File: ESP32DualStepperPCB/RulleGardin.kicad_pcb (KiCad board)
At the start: 2 copper layers, 56 x 33 mm, 20 parts, among them J1 Power, J2 Prog, J3 Conn_01x05, U1 ESP32-S2-WROVER, U2 TSR_1-2433, U3 ULN2003A, U4 AZ1117-3.3

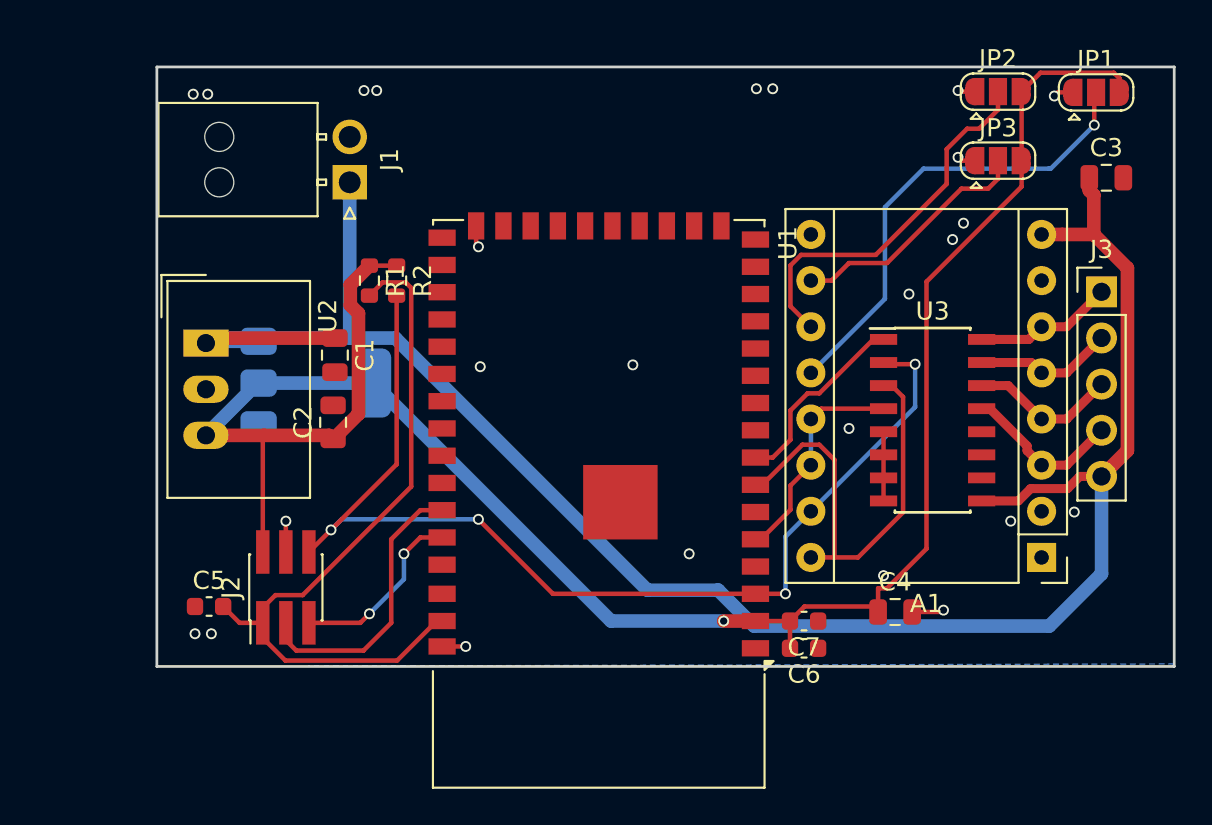
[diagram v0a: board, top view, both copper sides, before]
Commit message: fund that its the dhcp that the problem, so now with static IP
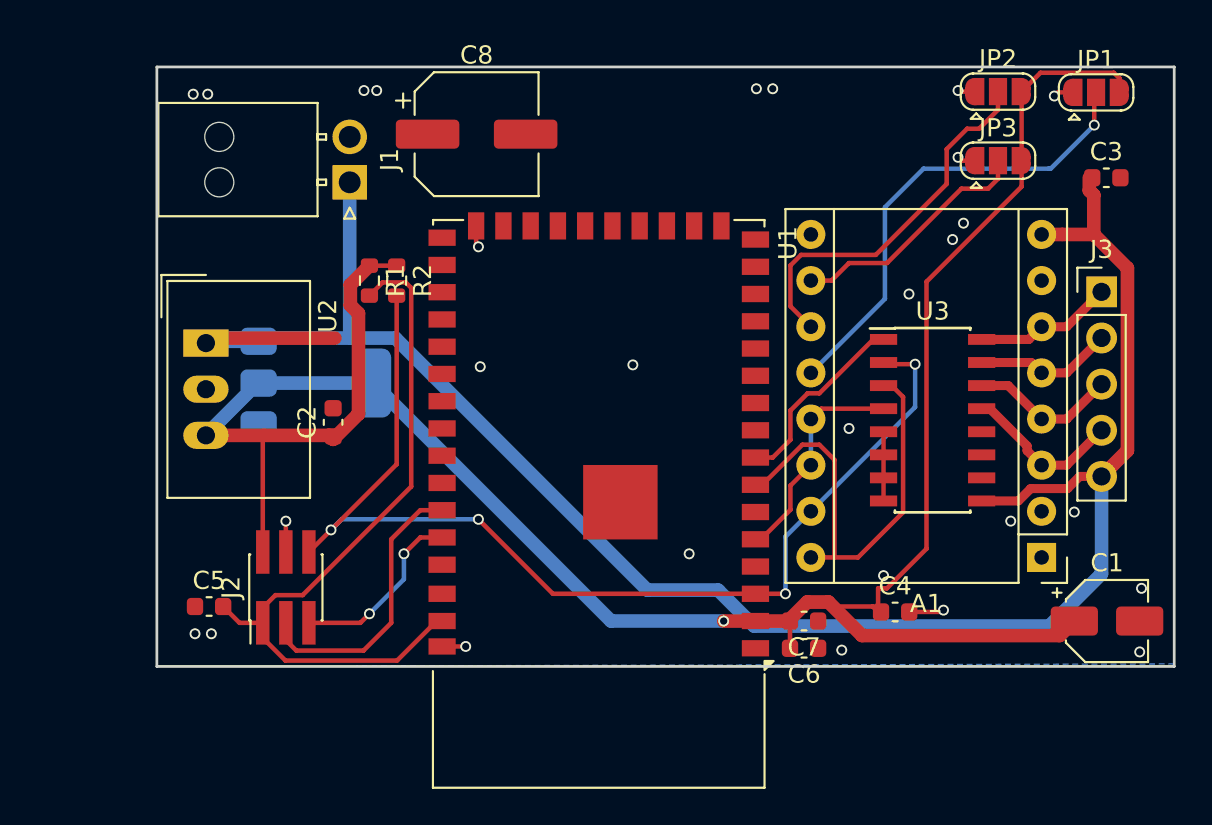
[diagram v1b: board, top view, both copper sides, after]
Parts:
- added C8: 10u, Capacitor_SMD:CP_Elec_6.3x7.7, F.Cu at (165.6, 89.7)
- C1: value 22uF -> 10u; footprint Capacitor_SMD:C_0805_2012Metric -> Capacitor_SMD:CP_Elec_4x5.4
- C2: value 22uF -> 1uF; footprint Capacitor_SMD:C_0805_2012Metric -> Capacitor_SMD:C_0603_1608Metric
- C3: footprint Capacitor_SMD:C_0805_2012Metric -> Capacitor_SMD:C_0603_1608Metric
- C4: value 1Uf -> 1uF; footprint Capacitor_SMD:C_0805_2012Metric -> Capacitor_SMD:C_0603_1608Metric
- moved C1 45.0 mm to (200.3, 116.5), turned to 0 degrees
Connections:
- C1 pad 1: +5V -> +3.3V
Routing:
- net +3.3V: track 110.3 -> 129.4 mm
- net GND: vias 25 -> 28

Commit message: updatePCB
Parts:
- moved J1 34.6 mm to (193.0, 88.5), turned to -90 degrees
- moved C7 33.7 mm to (149.9, 117.6), turned to 0 degrees
- moved U2 29.7 mm to (177.6, 88.7), turned to 180 degrees
- moved C5 26.7 mm to (155.4, 89.4), turned to 180 degrees
- moved JP1 25.7 mm to (178.7, 102.2), turned to 90 degrees
- moved J2 23.6 mm to (151.2, 91.3), turned to -90 degrees
- moved C8 20.5 mm to (186.1, 89.9), turned to 180 degrees
- moved U4 20.1 mm to (175.2, 95.5), turned to -90 degrees
- moved JP2 18.7 mm to (181.2, 100.7), turned to 90 degrees
- moved C2 17.3 mm to (171.7, 95.3), turned to 180 degrees
- moved JP3 17.0 mm to (178.6, 97.6), turned to 90 degrees
- moved U1 11.5 mm to (160.9, 107.2), turned to 90 degrees
- moved R1 8.14 mm to (155.3, 90.9), turned to 180 degrees
- moved R2 7.95 mm to (155.3, 92.4), turned to 180 degrees
- moved C3 7.10 mm to (194.6, 96.4), turned to -90 degrees
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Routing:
- net +5V: track 109.2 -> 57.9 mm
- net /D2: track 12.3 -> 47.4 mm, vias 0 -> 1
- net /D5: track 10.7 -> 44.5 mm
- net EN: track 40.1 -> 15.7 mm
- net +3.3V: track 129.4 -> 153.5 mm, vias 1 -> 2
- net Net-(A1-M2): track 26.0 -> 5.61 mm, vias 1 -> 0
- net Net-(A1-M1): track 20.9 -> 3.01 mm
- net /D4: track 24.8 -> 41.0 mm
- net D0: track 60.4 -> 75.1 mm, vias 4 -> 2
- net RX: track 10.1 -> 21.6 mm
- net Net-(A1-M0): track 13.6 -> 5.47 mm
- net GND: track 12.8 -> 18.8 mm, vias 28 -> 12
- net TX: track 15.7 -> 17.6 mm
- net /Coil3: track 7.63 -> 8.25 mm

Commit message: med device understøttelse
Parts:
- C6: value 100n -> 0.1uf
- C7: value 1uF -> 0.1uf
- U1: value ESP32-S2-WROVER -> ESP32-WROOM-32; footprint RF_Module:ESP32-S2-WROVER -> RF_Module:ESP32-WROOM-32
- moved U1 3.50 mm to (157.6, 106.0)
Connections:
- net /ESP32/GPIO37 renamed /ESP32/GPIO19
- net /ESP32/GPIO6 renamed /ESP32/GPIO33
- net /ESP32/GPIO7 renamed /ESP32/GPIO25
- net /ESP32/GPIO8 renamed /ESP32/GPIO26
- net /ESP32/GPIO9 renamed /ESP32/GPIO27
- U1 pad 13: /ESP32/GPIO10 -> /ESP32/GPIO14
- U1 pad 14: /ESP32/GPIO11 -> /ESP32/GPIO12
- U1 pad 15: /ESP32/GPIO12 -> GND
- U1 pad 17: /ESP32/GPIO14 -> unconnected-(U1-SHD/SD2-Pad17)
- U1 pad 18: /ESP32/GPIO15 -> unconnected-(U1-SWP/SD3-Pad18)
- U1 pad 19: /ESP32/GPIO16 -> unconnected-(U1-SCS/CMD-Pad19)
- U1 pad 20: /ESP32/GPIO17 -> unconnected-(U1-SCK/CLK-Pad20)
- U1 pad 21: /ESP32/GPIO18 -> unconnected-(U1-SDO/SD0-Pad21)
- U1 pad 23: unconnected-(U1-USB_D+-Pad23) -> /ESP32/GPIO15
- U1 pad 24: unconnected-(U1-IO21-Pad24) -> /D2
- U1 pad 25: unconnected-(U1-IO26-Pad25) -> D0
- U1 pad 26: GND -> /D4
- U1 pad 27: unconnected-(U1-IO33-Pad27) -> /ESP32/GPIO16
- U1 pad 28: unconnected-(U1-IO34-Pad28) -> /ESP32/GPIO17
- U1 pad 29: /ESP32/GPIO35 -> /D5
- U1 pad 3: D0 -> EN
- U1 pad 30: unconnected-(U1-IO36-Pad30) -> /ESP32/GPIO18
- U1 pad 32: /ESP32/GPIO38 -> unconnected-(U1-NC-Pad32)
- U1 pad 33: unconnected-(U1-IO39-Pad33) -> /ESP32/GPIO21
- U1 pad 34: /ESP32/GPIO40 -> RX
- U1 pad 35: unconnected-(U1-IO41-Pad35) -> TX
- U1 pad 36: unconnected-(U1-IO42-Pad36) -> /ESP32/SCL
- U1 pad 37: TX -> /ESP32/SDA
- U1 pad 38: RX -> GND
- U1 pad 39: unconnected-(U1-IO45-Pad39) -> GND
- U1 pad 5: /D2 -> unconnected-(U1-SENSOR_VN-Pad5)
- U1 pad 6: unconnected-(U1-IO03-Pad6) -> /ESP32/GPIO34
- U1 pad 7: /D4 -> /ESP32/GPIO35
- U1 pad 8: /D5 -> /ESP32/GPIO32
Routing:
- net D0: track 75.1 -> 56.2 mm, vias 2 -> 1
- net /D5: track 44.5 -> 29.6 mm, vias 0 -> 2
- net EN: track 15.7 -> 30.6 mm, vias 0 -> 2
- net /D2: track 47.4 -> 33.3 mm
- net TX: track 17.6 -> 12.2 mm
- net +3.3V: track 153.5 -> 154.5 mm
- net RX: track 21.6 -> 20.6 mm
- net GND: track 18.8 -> 18.2 mm, vias 12 -> 11
- net /D4: track 41.0 -> 40.9 mm, vias 0 -> 2
